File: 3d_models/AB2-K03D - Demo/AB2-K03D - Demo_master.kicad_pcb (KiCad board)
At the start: 2 copper layers, 234 parts

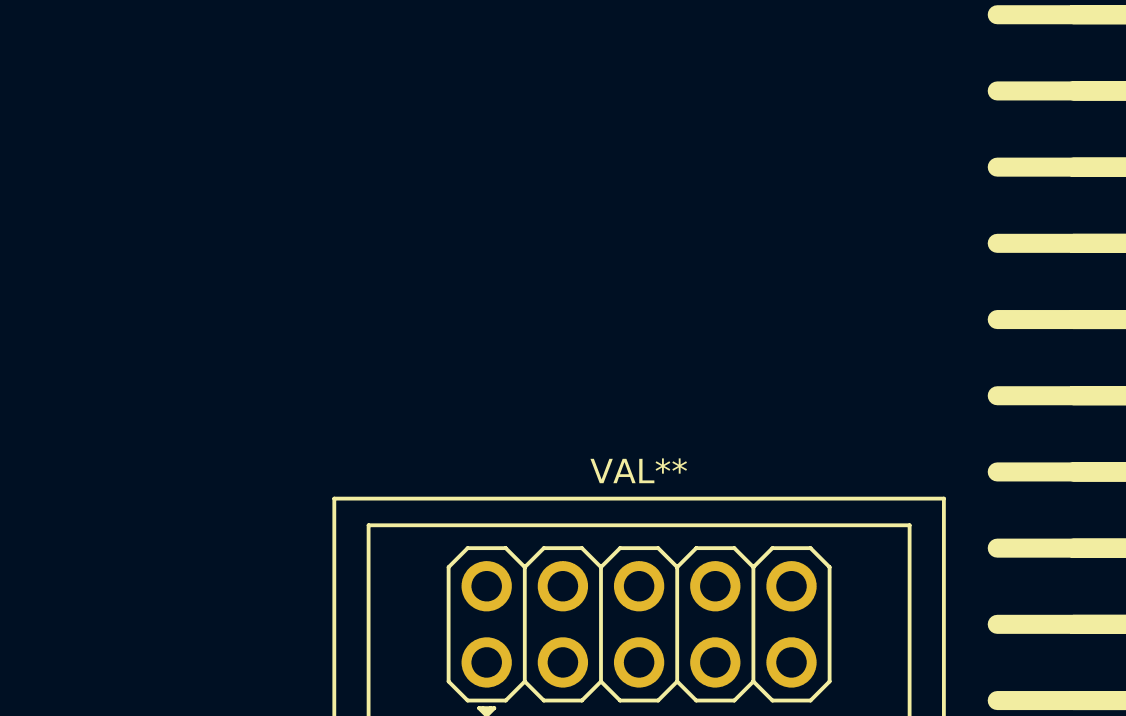
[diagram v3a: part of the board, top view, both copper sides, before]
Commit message: 3d: AB2-K03D: add 7pin idc shroud hdr
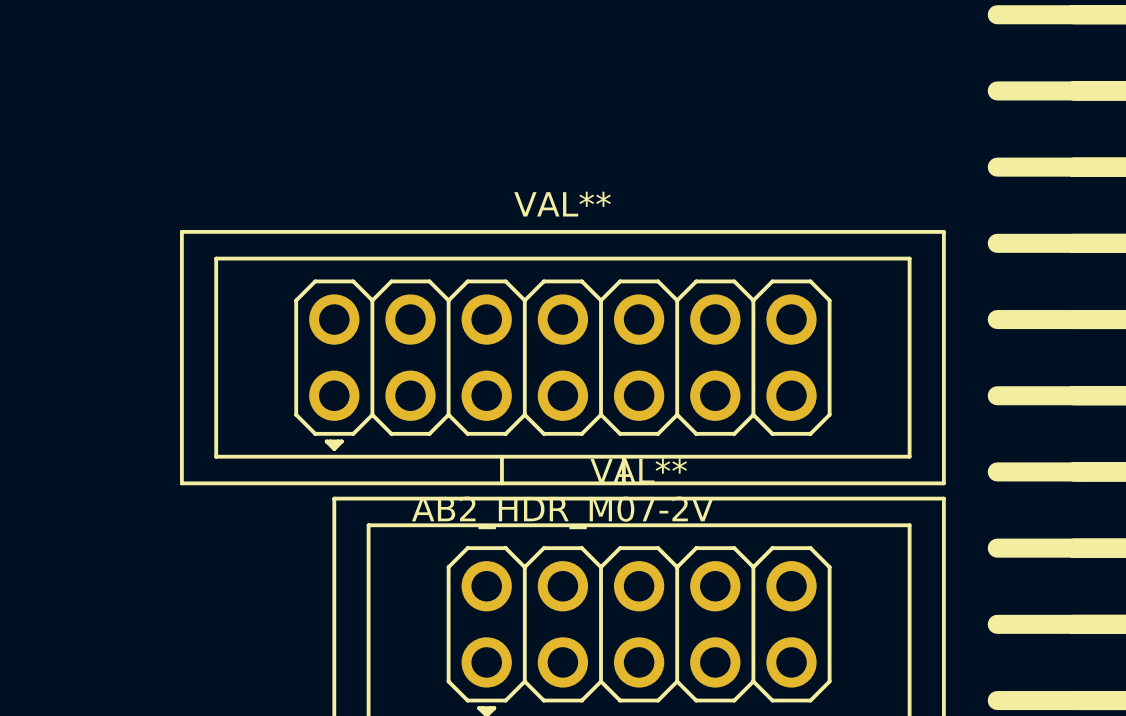
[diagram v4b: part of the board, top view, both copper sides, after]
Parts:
- added AB2_HDR_M07-2V: VAL**, AB2_HDR_M07-2V-S, F.Cu at (201.9, 152.4)
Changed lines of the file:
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@@
     (tracks 0)
     (zones 0)
-    (modules 234)
+    (modules 235)
     (nets 1)
   )
@@
     )
   )
+  (module AB2_HDR_M07-2V-S (layer F.Cu)
+    (at 201.93 152.4)
+    (path AB2_HDR07_2)
+    (fp_text reference AB2_HDR_M07-2V (at 0 5.08) (layer F.SilkS)
+      (effects (font (size 0.8128 0.8128) (thickness 0.0762)))
+    )
+    (fp_text value VAL** (at 0 -5.08) (layer F.SilkS)
+      (effects (font (size 0.8128 0.8128) (thickness 0.0762)))
+    )
+    (fp_line (start 2.032 3.302) (end 2.032 4.191) (layer F.SilkS) (width 0.127))
+    (fp_line (start -2.032 3.302) (end -2.032 4.191) (layer F.SilkS) (width 0.127))
+    (fp_line (start -7.493 2.794) (end -7.62 2.921) (layer F.SilkS) (width 0.127))
+    (fp_line (start -7.747 2.794) (end -7.62 2.921) (layer F.SilkS) (width 0.127))
+    (fp_line (start -7.874 2.794) (end -7.62 3.048) (layer F.SilkS) (width 0.127))
+    (fp_line (start -7.62 3.048) (end -7.366 2.794) (layer F.SilkS) (width 0.127))
+    (fp_line (start -7.366 2.794) (end -7.874 2.794) (layer F.SilkS) (width 0.127))
+    (fp_line (start 12.7 -4.191) (end 12.7 4.191) (layer F.SilkS) (width 0.127))
+    (fp_line (start 12.7 4.191) (end -12.7 4.191) (layer F.SilkS) (width 0.127))
+    (fp_line (start -12.7 4.191) (end -12.7 -4.191) (layer F.SilkS) (width 0.127))
+    (fp_line (start -12.7 -4.191) (end 12.7 -4.191) (layer F.SilkS) (width 0.127))
+    (fp_line (start 11.557 -3.302) (end 11.557 3.302) (layer F.SilkS) (width 0.127))
+    (fp_line (start -11.557 -3.302) (end -11.557 3.302) (layer F.SilkS) (width 0.127))
+    (fp_line (start 11.557 3.302) (end -11.557 3.302) (layer F.SilkS) (width 0.127))
+    (fp_line (start -11.557 -3.302) (end 11.557 -3.302) (layer F.SilkS) (width 0.127))
+    (fp_line (start 6.35 -1.905) (end 6.985 -2.54) (layer F.SilkS) (width 0.127))
+    (fp_line (start 6.985 -2.54) (end 8.255 -2.54) (layer F.SilkS) (width 0.127))
+    (fp_line (start 8.255 -2.54) (end 8.89 -1.905) (layer F.SilkS) (width 0.127))
+    (fp_line (start 8.89 -1.905) (end 8.89 1.905) (layer F.SilkS) (width 0.127))
+    (fp_line (start 8.89 1.905) (end 8.255 2.54) (layer F.SilkS) (width 0.127))
+    (fp_line (start 8.255 2.54) (end 6.985 2.54) (layer F.SilkS) (width 0.127))
+    (fp_line (start 6.985 2.54) (end 6.35 1.905) (layer F.SilkS) (width 0.127))
+    (fp_line (start 3.81 -1.905) (end 4.445 -2.54) (layer F.SilkS) (width 0.127))
+    (fp_line (start 4.445 -2.54) (end 5.715 -2.54) (layer F.SilkS) (width 0.127))
+    (fp_line (start 5.715 -2.54) (end 6.35 -1.905) (layer F.SilkS) (width 0.127))
+    (fp_line (start 6.35 -1.905) (end 6.35 1.905) (layer F.SilkS) (width 0.127))
+    (fp_line (start 6.35 1.905) (end 5.715 2.54) (layer F.SilkS) (width 0.127))
+    (fp_line (start 5.715 2.54) (end 4.445 2.54) (layer F.SilkS) (width 0.127))
+    (fp_line (start 4.445 2.54) (end 3.81 1.905) (layer F.SilkS) (width 0.127))
+    (fp_line (start 1.27 -1.905) (end 1.905 -2.54) (layer F.SilkS) (width 0.127))
+    (fp_line (start 1.905 -2.54) (end 3.175 -2.54) (layer F.SilkS) (width 0.127))
+    (fp_line (start 3.175 -2.54) (end 3.81 -1.905) (layer F.SilkS) (width 0.127))
+    (fp_line (start 3.81 -1.905) (end 3.81 1.905) (layer F.SilkS) (width 0.127))
+    (fp_line (start 3.81 1.905) (end 3.175 2.54) (layer F.SilkS) (width 0.127))
+    (fp_line (start 3.175 2.54) (end 1.905 2.54) (layer F.SilkS) (width 0.127))
+    (fp_line (start 1.905 2.54) (end 1.27 1.905) (layer F.SilkS) (width 0.127))
+    (fp_line (start -1.27 -1.905) (end -0.635 -2.54) (layer F.SilkS) (width 0.127))
+    (fp_line (start -0.635 -2.54) (end 0.635 -2.54) (layer F.SilkS) (width 0.127))
+    (fp_line (start 0.635 -2.54) (end 1.27 -1.905) (layer F.SilkS) (width 0.127))
+    (fp_line (start 1.27 -1.905) (end 1.27 1.905) (layer F.SilkS) (width 0.127))
+    (fp_line (start 1.27 1.905) (end 0.635 2.54) (layer F.SilkS) (width 0.127))
+    (fp_line (start 0.635 2.54) (end -0.635 2.54) (layer F.SilkS) (width 0.127))
+    (fp_line (start -0.635 2.54) (end -1.27 1.905) (layer F.SilkS) (width 0.127))
+    (fp_line (start -3.81 -1.905) (end -3.175 -2.54) (layer F.SilkS) (width 0.127))
+    (fp_line (start -3.175 -2.54) (end -1.905 -2.54) (layer F.SilkS) (width 0.127))
+    (fp_line (start -1.905 -2.54) (end -1.27 -1.905) (layer F.SilkS) (width 0.127))
+    (fp_line (start -1.27 -1.905) (end -1.27 1.905) (layer F.SilkS) (width 0.127))
+    (fp_line (start -1.27 1.905) (end -1.905 2.54) (layer F.SilkS) (width 0.127))
+    (fp_line (start -1.905 2.54) (end -3.175 2.54) (layer F.SilkS) (width 0.127))
+    (fp_line (start -3.175 2.54) (end -3.81 1.905) (layer F.SilkS) (width 0.127))
+    (fp_line (start -6.35 -1.905) (end -5.715 -2.54) (layer F.SilkS) (width 0.127))
+    (fp_line (start -5.715 -2.54) (end -4.445 -2.54) (layer F.SilkS) (width 0.127))
+    (fp_line (start -4.445 -2.54) (end -3.81 -1.905) (layer F.SilkS) (width 0.127))
+    (fp_line (start -3.81 -1.905) (end -3.81 1.905) (layer F.SilkS) (width 0.127))
+    (fp_line (start -3.81 1.905) (end -4.445 2.54) (layer F.SilkS) (width 0.127))
+    (fp_line (start -4.445 2.54) (end -5.715 2.54) (layer F.SilkS) (width 0.127))
+    (fp_line (start -5.715 2.54) (end -6.35 1.905) (layer F.SilkS) (width 0.127))
+    (fp_line (start -8.255 2.54) (end -8.89 1.905) (layer F.SilkS) (width 0.127))
+    (fp_line (start -8.89 1.905) (end -8.89 -1.905) (layer F.SilkS) (width 0.127))
+    (fp_line (start -8.89 -1.905) (end -8.255 -2.54) (layer F.SilkS) (width 0.127))
+    (fp_line (start -8.255 -2.54) (end -6.985 -2.54) (layer F.SilkS) (width 0.127))
+    (fp_line (start -6.985 -2.54) (end -6.35 -1.905) (layer F.SilkS) (width 0.127))
+    (fp_line (start -6.35 -1.905) (end -6.35 1.905) (layer F.SilkS) (width 0.127))
+    (fp_line (start -6.35 1.905) (end -6.985 2.54) (layer F.SilkS) (width 0.127))
+    (fp_line (start -6.985 2.54) (end -8.255 2.54) (layer F.SilkS) (width 0.127))
+    (pad 1 thru_hole circle (at -7.62 1.27) (size 1.6764 1.6764) (drill 1.016)
+      (layers *.Cu *.Mask F.SilkS)
+    )
+    (pad 2 thru_hole circle (at -7.62 -1.27) (size 1.6764 1.6764) (drill 1.016)
+      (layers *.Cu *.Mask F.SilkS)
+    )
+    (pad 3 thru_hole circle (at -5.08 1.27) (size 1.6764 1.6764) (drill 1.016)
+      (layers *.Cu *.Mask F.SilkS)
+    )
+    (pad 4 thru_hole circle (at -5.08 -1.27) (size 1.6764 1.6764) (drill 1.016)
+      (layers *.Cu *.Mask F.SilkS)
+    )
+    (pad 5 thru_hole circle (at -2.54 1.27) (size 1.6764 1.6764) (drill 1.016)
+      (layers *.Cu *.Mask F.SilkS)
+    )
+    (pad 6 thru_hole circle (at -2.54 -1.27) (size 1.6764 1.6764) (drill 1.016)
+      (layers *.Cu *.Mask F.SilkS)
+    )
+    (pad 7 thru_hole circle (at 0 1.27) (size 1.6764 1.6764) (drill 1.016)
+      (layers *.Cu *.Mask F.SilkS)
+    )
+    (pad 8 thru_hole circle (at 0 -1.27) (size 1.6764 1.6764) (drill 1.016)
+      (layers *.Cu *.Mask F.SilkS)
+    )
+    (pad 9 thru_hole circle (at 2.54 1.27) (size 1.6764 1.6764) (drill 1.016)
+      (layers *.Cu *.Mask F.SilkS)
+    )
+    (pad 10 thru_hole circle (at 2.54 -1.27) (size 1.6764 1.6764) (drill 1.016)
+      (layers *.Cu *.Mask F.SilkS)
+    )
+    (pad 11 thru_hole circle (at 5.08 1.27) (size 1.6764 1.6764) (drill 1.016)
+      (layers *.Cu *.Mask F.SilkS)
+    )
+    (pad 12 thru_hole circle (at 5.08 -1.27) (size 1.6764 1.6764) (drill 1.016)
+      (layers *.Cu *.Mask F.SilkS)
+    )
+    (pad 13 thru_hole circle (at 7.62 1.27) (size 1.6764 1.6764) (drill 1.016)
+      (layers *.Cu *.Mask F.SilkS)
+    )
+    (pad 14 thru_hole circle (at 7.62 -1.27) (size 1.6764 1.6764) (drill 1.016)
+      (layers *.Cu *.Mask F.SilkS)
+    )
+    (model ../3d_models/ab2_idc/AB2_HDR_M07-2V-S-3M.wrl
+      (at (xyz 0 0 0))
+      (scale (xyz 0.3937 0.3937 0.3937))
+      (rotate (xyz 0 0 0))
+    )
+  )
